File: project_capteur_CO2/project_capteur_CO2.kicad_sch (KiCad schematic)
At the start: 7 parts

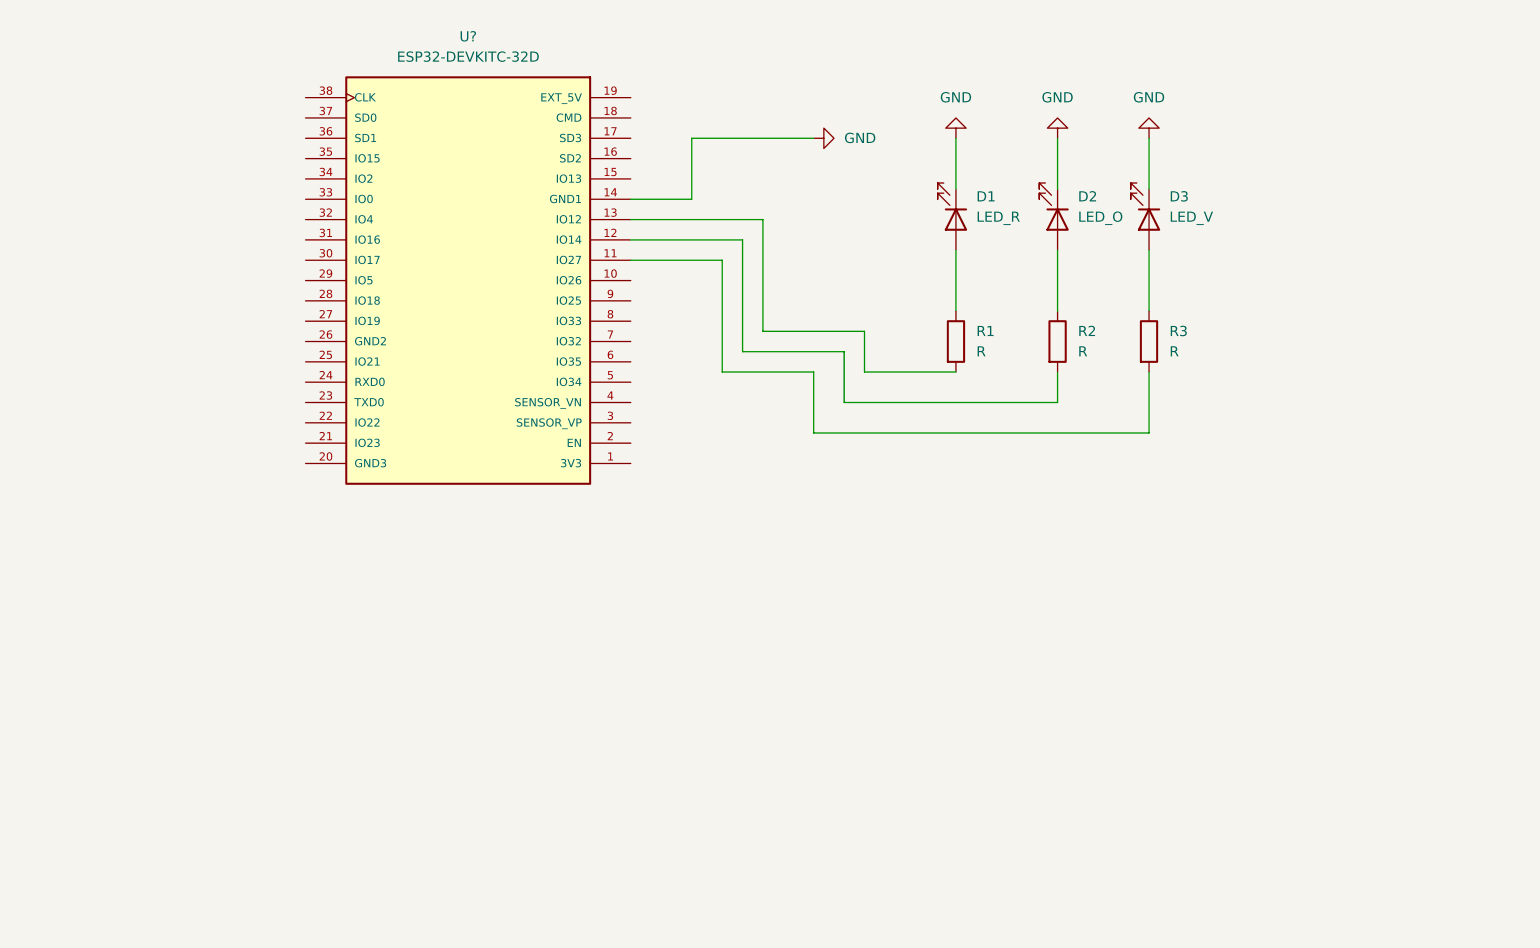
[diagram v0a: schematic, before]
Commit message: schéma et empreinte fait mais empreinte capteur à refaire
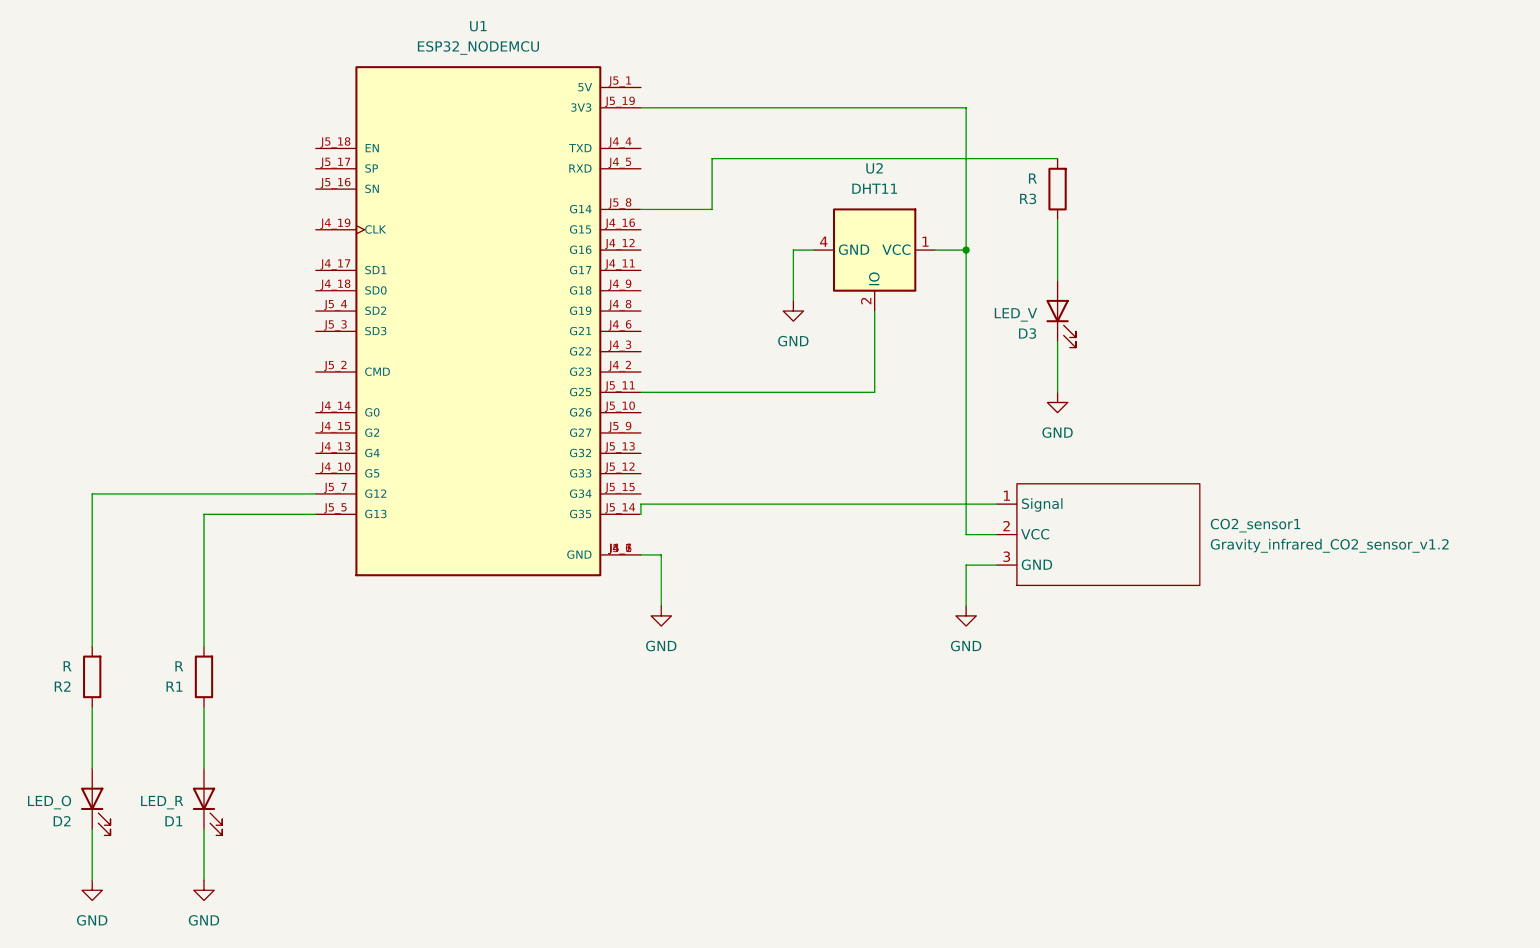
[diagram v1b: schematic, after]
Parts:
- removed U?: ESP32-DEVKITC-32D, MODULE_ESP32-DEVKITC-32D, symbol ESP32-DEVKITC-32D:ESP32-DEVKITC-32D
- added CO2_sensor1: Gravity_infrared_CO2_sensor_v1.2, Gravity infrared co2 sensor v1:Sensor_CO2_3pins_37mmx69mm, symbol sensor_infrared_co2:Gravity_infrared_CO2_sensor_v1.2
- added U1: ESP32_NODEMCU, ESP32_NODEMCU:MODULE_ESP32_NODEMCU, symbol ESP32_NODEMCU:ESP32_NODEMCU
- added U2: DHT11, Sensor:Aosong_DHT11_5.5x12.0_P2.54mm, symbol Sensor:DHT11
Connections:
- net GND: now also CO2_sensor1.3 (GND), U1.J4_1 (GND), U1.J4_7 (GND), U1.J5_6 (GND), U2.4 (GND)
- net at R2.2: now also U1.J5_7 (G12)
- net at R3.2: now also U1.J5_8 (G14)
- net at R1.2: now also U1.J5_5 (G13)
- new net: CO2_sensor1.1 (Signal), U1.J5_14 (G35)
- new net: CO2_sensor1.2 (VCC), U1.J5_19 (3V3), U2.1 (VCC)
- new net: U1.J5_11 (G25), U2.2 (IO)
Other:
- moved on the sheet: D1, D2, D3, R1, R2, R3

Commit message: pinheader - coorection led empreinte ajouter
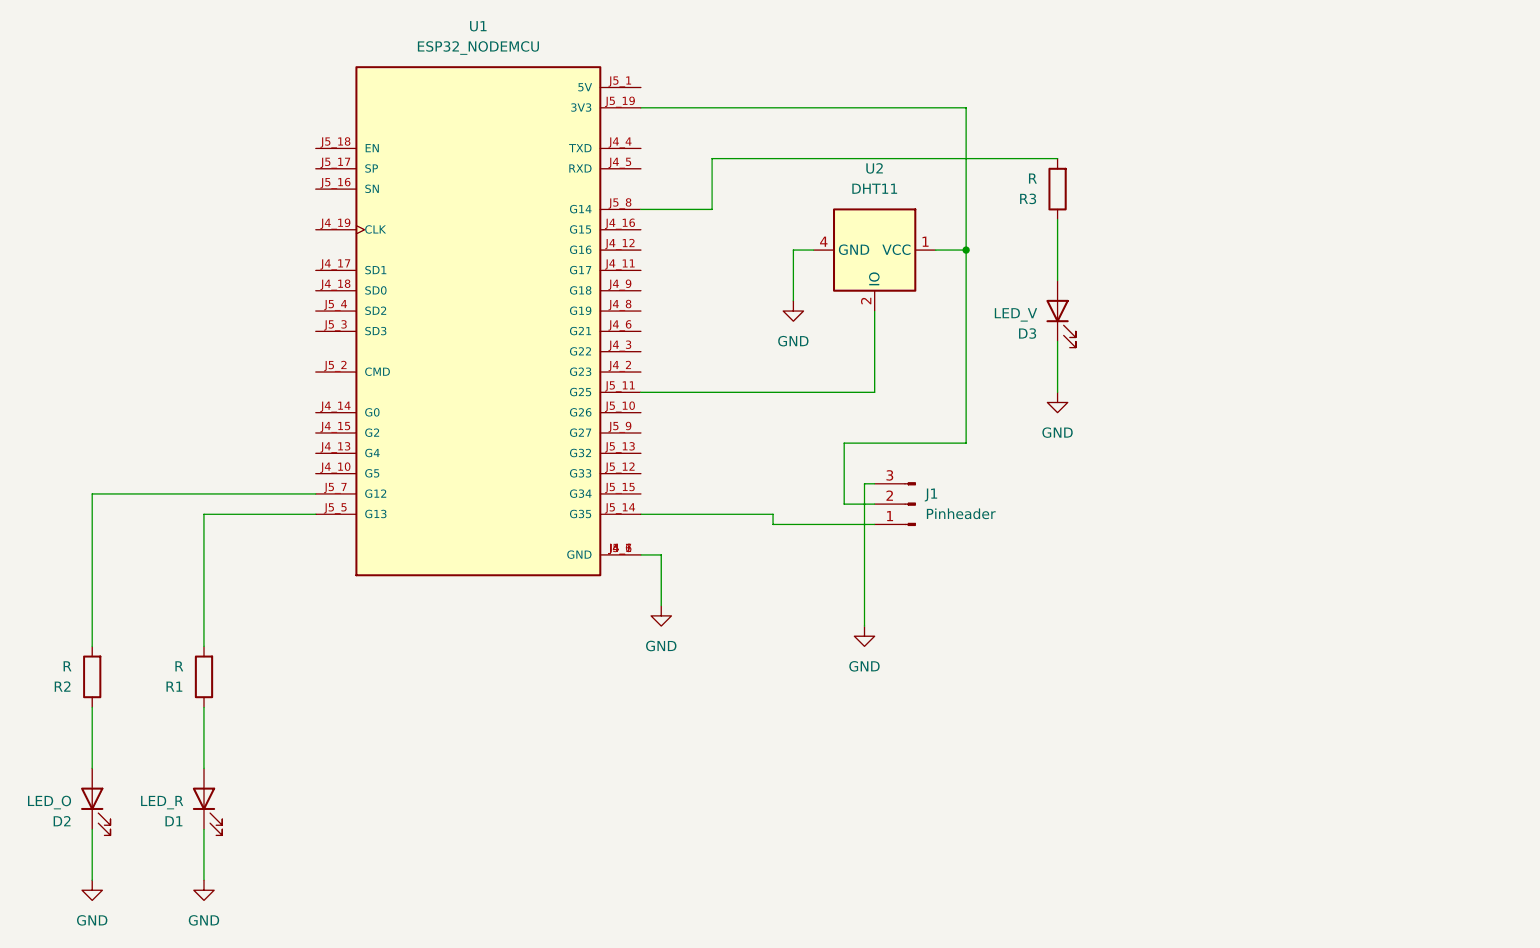
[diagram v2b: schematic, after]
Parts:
- removed CO2_sensor1: Gravity_infrared_CO2_sensor_v1.2, Gravity infrared co2 sensor v1:Sensor_CO2_3pins_37mmx69mm, symbol sensor_infrared_co2:Gravity_infrared_CO2_sensor_v1.2
- added J1: Pinheader, Connector_PinHeader_1.00mm:PinHeader_1x03_P1.00mm_Vertical, symbol Connector:Conn_01x03_Male
- D1, D2, D3: footprint LED_SMD:LED_miniPLCC_2315 -> LED_THT:LED_D3.0mm
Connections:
- net GND: now also J1.3 (Pin_3)
- net at U1.J5_14 (G35): now also J1.1 (Pin_1)
- net at U1.J5_19 (3V3), U2.1 (VCC): now also J1.2 (Pin_2)
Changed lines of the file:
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@@
-    (stroke (width 0) (type default) (color 0 0 0 0))
-  )
-  (wire (pts (xy 97.79 97.79) (xy 97.79 99.06))
     (stroke (width 0) (type default) (color 0 0 0 0))
   )
@@
     (stroke (width 0) (type default) (color 0 0 0 0))
   )
+  (wire (pts (xy 123.19 90.17) (xy 138.43 90.17))
+    (stroke (width 0) (type default) (color 0 0 0 0))
+  )
   (wire (pts (xy 29.21 96.52) (xy 57.15 96.52))
     (stroke (width 0) (type default) (color 0 0 0 0))
   )
+  (wire (pts (xy 127 97.79) (xy 123.19 97.79))
+    (stroke (width 0) (type default) (color 0 0 0 0))
+  )
+  (wire (pts (xy 114.3 100.33) (xy 127 100.33))
+    (stroke (width 0) (type default) (color 0 0 0 0))
+  )
+  (wire (pts (xy 138.43 90.17) (xy 138.43 66.04))
+    (stroke (width 0) (type default) (color 0 0 0 0))
+  )
   (wire (pts (xy 127 83.82) (xy 97.79 83.82))
     (stroke (width 0) (type default) (color 0 0 0 0))
@@
     (stroke (width 0) (type default) (color 0 0 0 0))
   )
-  (wire (pts (xy 138.43 105.41) (xy 138.43 110.49))
+  (wire (pts (xy 97.79 99.06) (xy 114.3 99.06))
     (stroke (width 0) (type default) (color 0 0 0 0))
   )
@@
     (stroke (width 0) (type default) (color 0 0 0 0))
   )
+  (wire (pts (xy 127 95.25) (xy 125.73 95.25))
+    (stroke (width 0) (type default) (color 0 0 0 0))
+  )
   (wire (pts (xy 149.86 69.85) (xy 149.86 62.23))
     (stroke (width 0) (type default) (color 0 0 0 0))
@@
     (stroke (width 0) (type default) (color 0 0 0 0))
   )
-  (wire (pts (xy 142.24 101.6) (xy 138.43 101.6))
+  (wire (pts (xy 125.73 95.25) (xy 125.73 113.03))
     (stroke (width 0) (type default) (color 0 0 0 0))
   )
@@
     (stroke (width 0) (type default) (color 0 0 0 0))
   )
-  (wire (pts (xy 138.43 66.04) (xy 138.43 101.6))
+  (wire (pts (xy 114.3 99.06) (xy 114.3 100.33))
     (stroke (width 0) (type default) (color 0 0 0 0))
   )
@@
     (stroke (width 0) (type default) (color 0 0 0 0))
   )
-  (wire (pts (xy 142.24 105.41) (xy 138.43 105.41))
-    (stroke (width 0) (type default) (color 0 0 0 0))
-  )
-  (wire (pts (xy 142.24 97.79) (xy 97.79 97.79))
+  (wire (pts (xy 123.19 97.79) (xy 123.19 90.17))
     (stroke (width 0) (type default) (color 0 0 0 0))
   )
@@
     (pin "1")
   )
+  (symbol (lib_id "Connector:Conn_01x03_Male") (at 132.08 97.79 180) (unit 1)
+    (in_bom yes) (on_board yes) (fields_autoplaced)
+    (property "Reference" "J1" (id 0) (at 133.35 96.5199 0)
+      (effects (font (size 1.27 1.27)) (justify right))
+    )
+    (property "Value" "Pinheader" (id 1) (at 133.35 99.0599 0)
+      (effects (font (size 1.27 1.27)) (justify right))
+    )
+    (property "Footprint" "Connector_PinHeader_1.00mm:PinHeader_1x03_P1.00mm_Vertical" (id 2) (at 132.08 97.79 0)
+      (effects (font (size 1.27 1.27)) hide)
+    )
+    (property "Datasheet" "~" (id 3) (at 132.08 97.79 0)
+      (effects (font (size 1.27 1.27)) hide)
+    )
+    (pin "1")
+    (pin "2")
+    (pin "3")
+  )
   (symbol (lib_id "Device:R") (at 149.86 58.42 180) (unit 1)
     (in_bom yes) (on_board yes) (fields_autoplaced)
@@
     (pin "1")
     (pin "2")
+  )
+  (symbol (lib_id "power:GND") (at 125.73 113.03 0) (unit 1)
+    (in_bom yes) (on_board yes) (fields_autoplaced)
+    (property "Reference" "#PWR0106" (id 0) (at 125.73 119.38 0)
+      (effects (font (size 1.27 1.27)) hide)
+    )
+    (property "Value" "GND" (id 1) (at 125.73 118.11 0))
+    (property "Footprint" "" (id 2) (at 125.73 113.03 0)
+      (effects (font (size 1.27 1.27)) hide)
+    )
+    (property "Datasheet" "" (id 3) (at 125.73 113.03 0)
+      (effects (font (size 1.27 1.27)) hide)
+    )
+    (pin "1")
   )
   (symbol (lib_id "Device:R") (at 43.18 119.38 180) (unit 1)
@@
       (effects (font (size 1.27 1.27)) (justify left))
     )
-    (property "Footprint" "LED_SMD:LED_miniPLCC_2315" (id 2) (at 149.86 73.66 0)
+    (property "Footprint" "LED_THT:LED_D3.0mm" (id 2) (at 149.86 73.66 0)
       (effects (font (size 1.27 1.27)) hide)
     )
@@
     (pin "1")
   )
-  (symbol (lib_id "sensor_infrared_co2:Gravity_infrared_CO2_sensor_v1.2") (at 143.51 97.79 0) (unit 1)
-    (in_bom yes) (on_board yes) (fields_autoplaced)
-    (property "Reference" "CO2_sensor1" (id 0) (at 168.91 100.3299 0)
-      (effects (font (size 1.27 1.27)) (justify left))
-    )
-    (property "Value" "Gravity_infrared_CO2_sensor_v1.2" (id 1) (at 168.91 102.8699 0)
-      (effects (font (size 1.27 1.27)) (justify left))
-    )
-    (property "Footprint" "Gravity infrared co2 sensor v1:Sensor_CO2_3pins_37mmx69mm" (id 2) (at 143.51 97.79 0)
-      (effects (font (size 1.27 1.27)) hide)
-    )
-    (property "Datasheet" "" (id 3) (at 143.51 97.79 0)
-      (effects (font (size 1.27 1.27)) hide)
-    )
-    (pin "1")
-    (pin "2")
-    (pin "3")
-  )
   (symbol (lib_id "power:GND") (at 100.33 110.49 0) (unit 1)
     (in_bom yes) (on_board yes) (fields_autoplaced)
@@
       (effects (font (size 1.27 1.27)) (justify left))
     )
-    (property "Footprint" "LED_SMD:LED_miniPLCC_2315" (id 2) (at 43.18 134.62 0)
+    (property "Footprint" "LED_THT:LED_D3.0mm" (id 2) (at 43.18 134.62 0)
       (effects (font (size 1.27 1.27)) hide)
     )
@@
       (effects (font (size 1.27 1.27)) (justify left))
     )
-    (property "Footprint" "LED_SMD:LED_miniPLCC_2315" (id 2) (at 29.21 134.62 0)
+    (property "Footprint" "LED_THT:LED_D3.0mm" (id 2) (at 29.21 134.62 0)
       (effects (font (size 1.27 1.27)) hide)
     )
@@
     (pin "4")
   )
-  (symbol (lib_id "power:GND") (at 138.43 110.49 0) (unit 1)
-    (in_bom yes) (on_board yes) (fields_autoplaced)
-    (property "Reference" "#PWR?" (id 0) (at 138.43 116.84 0)
-      (effects (font (size 1.27 1.27)) hide)
-    )
-    (property "Value" "GND" (id 1) (at 138.43 115.57 0))
-    (property "Footprint" "" (id 2) (at 138.43 110.49 0)
-      (effects (font (size 1.27 1.27)) hide)
-    )
-    (property "Datasheet" "" (id 3) (at 138.43 110.49 0)
-      (effects (font (size 1.27 1.27)) hide)
-    )
-    (pin "1")
-  )
   (symbol (lib_id "power:GND") (at 149.86 83.82 0) (unit 1)
     (in_bom yes) (on_board yes) (fields_autoplaced)
@@
       (reference "#PWR0105") (unit 1) (value "GND") (footprint "")
     )
-    (path "/dbe691d4-022e-4219-8c53-de30d3e1b0cd"
-      (reference "#PWR?") (unit 1) (value "GND") (footprint "")
-    )
-    (path "/622991a4-7176-4bc5-949f-0d0fdab4c287"
-      (reference "CO2_sensor1") (unit 1) (value "Gravity_infrared_CO2_sensor_v1.2") (footprint "Gravity infrared co2 sensor v1:Sensor_CO2_3pins_37mmx69mm")
+    (path "/3341216b-e445-429b-bca7-8ec94be06d9e"
+      (reference "#PWR0106") (unit 1) (value "GND") (footprint "")
     )
     (path "/81de4538-8fea-4609-9a1e-73523faded18"
-      (reference "D1") (unit 1) (value "LED_R") (footprint "LED_SMD:LED_miniPLCC_2315")
+      (reference "D1") (unit 1) (value "LED_R") (footprint "LED_THT:LED_D3.0mm")
     )
     (path "/88689a38-8f9b-413b-a84a-3c7e6cac0080"
-      (reference "D2") (unit 1) (value "LED_O") (footprint "LED_SMD:LED_miniPLCC_2315")
+      (reference "D2") (unit 1) (value "LED_O") (footprint "LED_THT:LED_D3.0mm")
     )
     (path "/3aed4a66-ba3d-4321-a84b-ec8d95b0de6c"
-      (reference "D3") (unit 1) (value "LED_V") (footprint "LED_SMD:LED_miniPLCC_2315")
+      (reference "D3") (unit 1) (value "LED_V") (footprint "LED_THT:LED_D3.0mm")
+    )
+    (path "/150c7323-b5dd-4cea-a480-9e754a04ad85"
+      (reference "J1") (unit 1) (value "Pinheader") (footprint "Connector_PinHeader_1.00mm:PinHeader_1x03_P1.00mm_Vertical")
     )
     (path "/38c24697-197b-4f2e-a0f5-b2b029ab5bbe"
